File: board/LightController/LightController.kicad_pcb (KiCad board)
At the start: 2 copper layers, 114.8 x 68.6 mm, 38 parts, among them J1 PJ-051AH, J2 Light bank 1, J3 Light Bank 2, J4 Light Bank 3, U1 CPC1002N, U10 CPC1002N, U11 CPC1002N, U12 FeatherS2, U2 CPC1002N, U3 CPC1002N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

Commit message: Changed Inductor value to 8.2µH.
Matches the component ordered as 8.7µH is an uncommon value.
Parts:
- L1: value 8.7µH -> 8.2µH
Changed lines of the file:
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@@
       (effects (font (size 1 1) (thickness 0.15)))
     )
-    (fp_text value "100nF" (at -4.318 -1.6455) (layer "F.Fab")
+    (fp_text value "100nF" (at -4.318 1.524) (layer "F.Fab")
       (effects (font (size 1 1) (thickness 0.15)))
     )
@@
       (effects (font (size 1 1) (thickness 0.15)))
     )
-    (fp_text value "8.7µH" (at -2.794 3.556) (layer "F.Fab")
+    (fp_text value "8.2µH" (at -2.794 3.556) (layer "F.Fab")
       (effects (font (size 1 1) (thickness 0.15)))
     )

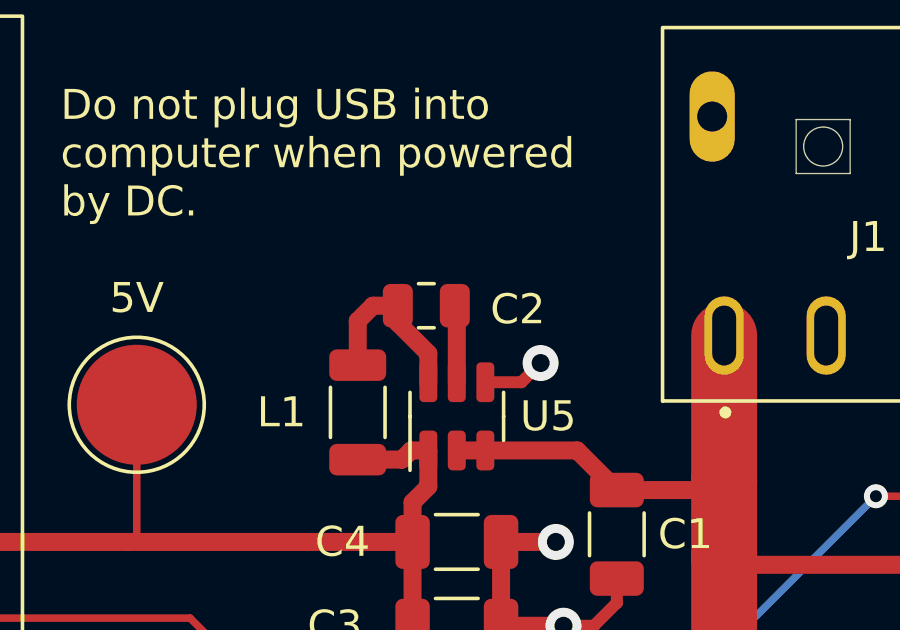
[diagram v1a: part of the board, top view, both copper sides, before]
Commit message: Fixed pin 5/6 swap design issue.
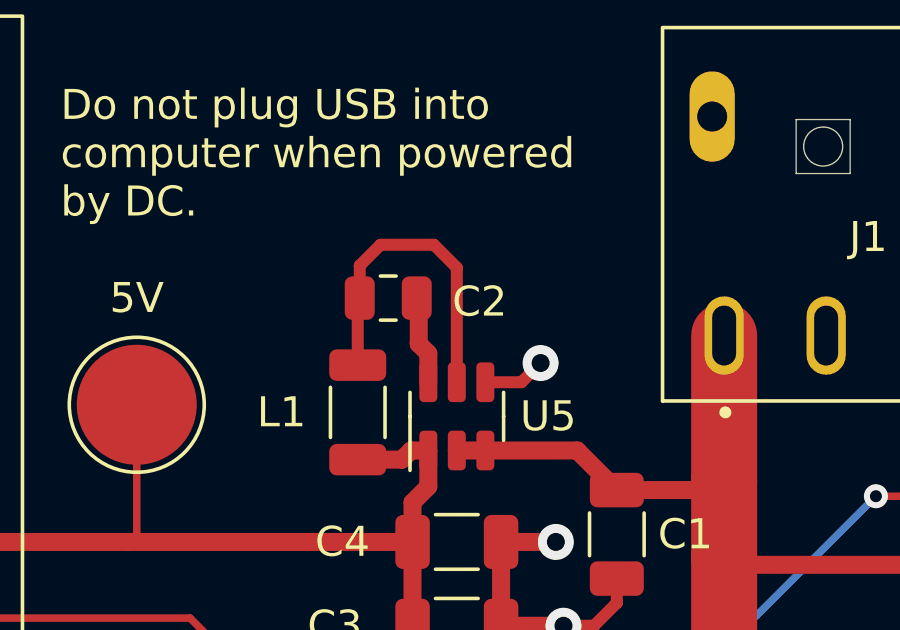
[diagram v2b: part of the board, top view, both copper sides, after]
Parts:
- moved C2 1.30 mm to (138.7, 59.9)
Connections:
- U5 pad 5: Net-(C2-Pad1) -> Net-(C2-Pad2)
- U5 pad 6: Net-(C2-Pad2) -> Net-(C2-Pad1)
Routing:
- net Net-(C2-Pad2): track 5.99 -> 11.0 mm
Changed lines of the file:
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@@
   )
   (footprint "Capacitor_SMD:C_0805_2012Metric" (layer "F.Cu")
-    (at 139.954 60.198 180)
+    (at 138.684 59.944 180)
     (descr "Capacitor SMD 0805 (2012 Metric), square (rectangular) end terminal, IPC_7351 nominal, (Body size source: IPC-SM-782 page 76, https://www.pcb-3d.com/wordpress/wp-content/uploads/ipc-sm-782a_amendment_1_and_2.pdf, https://docs.google.com/spreadsheets/d/1BsfQQcO9C6DZCsRaXUlFlo91Tg2WpOkGARC1WS5S8t0/edit?usp=sharing), generated with kicad-footprint-generator")
     (tags "capacitor")
@@
       (net 2 "GND") (pinfunction "GND") (pintype "power_in"))
     (pad "5" smd roundrect (at 1.1375 0 90) (size 1.325 0.6) (layers "F.Cu" "F.Paste" "F.Mask") (roundrect_rratio 0.25)
-      (net 3 "Net-(C2-Pad1)") (pinfunction "SW") (pintype "output"))
+      (net 4 "Net-(C2-Pad2)") (pinfunction "SW") (pintype "output"))
     (pad "6" smd roundrect (at 1.1375 -0.95 90) (size 1.325 0.6) (layers "F.Cu" "F.Paste" "F.Mask") (roundrect_rratio 0.25)
-      (net 4 "Net-(C2-Pad2)") (pinfunction "BST") (pintype "passive"))
+      (net 3 "Net-(C2-Pad1)") (pinfunction "BST") (pintype "passive"))
     (model "${KICAD6_3DMODEL_DIR}/Package_TO_SOT_SMD.3dshapes/TSOT-23-6.wrl"
       (offset (xyz 0 0 0))
@@
   (via (at 171.958 98.806) (size 1.2) (drill 0.6) (layers "F.Cu" "B.Cu") (net 2))
   (via (at 144.526 70.866) (size 1.2) (drill 0.6) (layers "F.Cu" "B.Cu") (net 2))
-  (segment (start 140.97 62.749) (end 140.97 60.264) (width 0.6) (layer "F.Cu") (net 3))
-  (segment (start 140.97 60.264) (end 140.904 60.198) (width 0.6) (layer "F.Cu") (net 3))
-  (segment (start 139.004 60.772) (end 140.02 61.788) (width 0.6) (layer "F.Cu") (net 4))
-  (segment (start 138.176 60.198) (end 137.668 60.706) (width 0.6) (layer "F.Cu") (net 4))
-  (segment (start 139.004 60.198) (end 139.004 60.772) (width 0.6) (layer "F.Cu") (net 4))
-  (segment (start 139.004 60.198) (end 138.176 60.198) (width 0.6) (layer "F.Cu") (net 4))
-  (segment (start 140.02 61.788) (end 140.02 62.749) (width 0.6) (layer "F.Cu") (net 4))
-  (segment (start 137.668 60.706) (end 137.668 62.179) (width 0.6) (layer "F.Cu") (net 4))
+  (segment (start 139.7 60.01) (end 139.634 59.944) (width 0.6) (layer "F.Cu") (net 3))
+  (segment (start 140.02 62.749) (end 140.02 61.788) (width 0.6) (layer "F.Cu") (net 3))
+  (segment (start 140.02 61.788) (end 139.7 61.468) (width 0.6) (layer "F.Cu") (net 3))
+  (segment (start 139.7 61.468) (end 139.7 60.01) (width 0.6) (layer "F.Cu") (net 3))
+  (segment (start 138.43 58.166) (end 137.734 58.862) (width 0.4) (layer "F.Cu") (net 4))
+  (segment (start 140.208 58.166) (end 138.43 58.166) (width 0.4) (layer "F.Cu") (net 4))
+  (segment (start 140.97 58.928) (end 140.208 58.166) (width 0.4) (layer "F.Cu") (net 4))
+  (segment (start 137.668 60.01) (end 137.734 59.944) (width 0.4) (layer "F.Cu") (net 4))
+  (segment (start 137.668 62.179) (end 137.668 60.01) (width 0.4) (layer "F.Cu") (net 4))
+  (segment (start 140.97 62.749) (end 140.97 58.928) (width 0.4) (layer "F.Cu") (net 4))
+  (segment (start 137.734 58.862) (end 137.734 59.944) (width 0.4) (layer "F.Cu") (net 4))
   (segment (start 140.02 66.228) (end 139.495 66.753) (width 0.6) (layer "F.Cu") (net 5))
   (segment (start 139.141 65.329) (end 137.668 65.329) (width 0.6) (layer "F.Cu") (net 5))
